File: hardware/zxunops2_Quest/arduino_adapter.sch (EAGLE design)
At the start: 8 parts

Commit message: Finalizo placa parte arduino
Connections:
- removed net D7: JP4.3
- removed net D8: JP4.2
- removed net M1+: JP4.4
- removed net M1-: JP4.5
- removed net M2+: JP5.12
- removed net M2-: JP5.11
- removed net MISO: JP5.10
- removed net N$10: JP11.5
- removed net N$6: JP11.1
- removed net N$7: JP11.2
- removed net N$8: JP11.3
- removed net N$9: JP11.4
- removed net PB1: JP4.1
- removed net SCK: JP5.9
- removed net SEN1: JP6.1
- removed net SEN10: JP6.14
- removed net SEN3: JP6.7
- removed net SEN4: JP5.8, JP6.9
- removed net SEN5: JP4.8, JP6.11
- removed net SEN6: JP6.4
- removed net SEN7: JP6.6
- removed net SEN8: JP4.6, JP6.10
- removed net SW1: JP5.7
- new net A10: JP4.7, JP6.2
- new net A11: JP4.8, JP6.1
- new net A12: JP4.5, JP6.4
- new net A13: JP4.4, JP6.5
- new net A14: JP4.2, JP6.7
- new net A15: JP4.1, JP6.8
- new net A8: JP4.3, JP6.6
- new net A9: JP4.6, JP6.3
- new net D0: JP11.1, JP5.7
- new net D1: JP11.2, JP5.8
- new net D2: JP11.3, JP5.10
- new net D4: JP11.5, JP5.12
- net 3.3V: no longer JP6.5
- net D3: now also JP11.4, JP5.11; no longer JP4.7
- net GND: now also MOUSE.3; no longer JP6.13, JP6.2, JP6.8
- net VCC: now also MOUSE.4

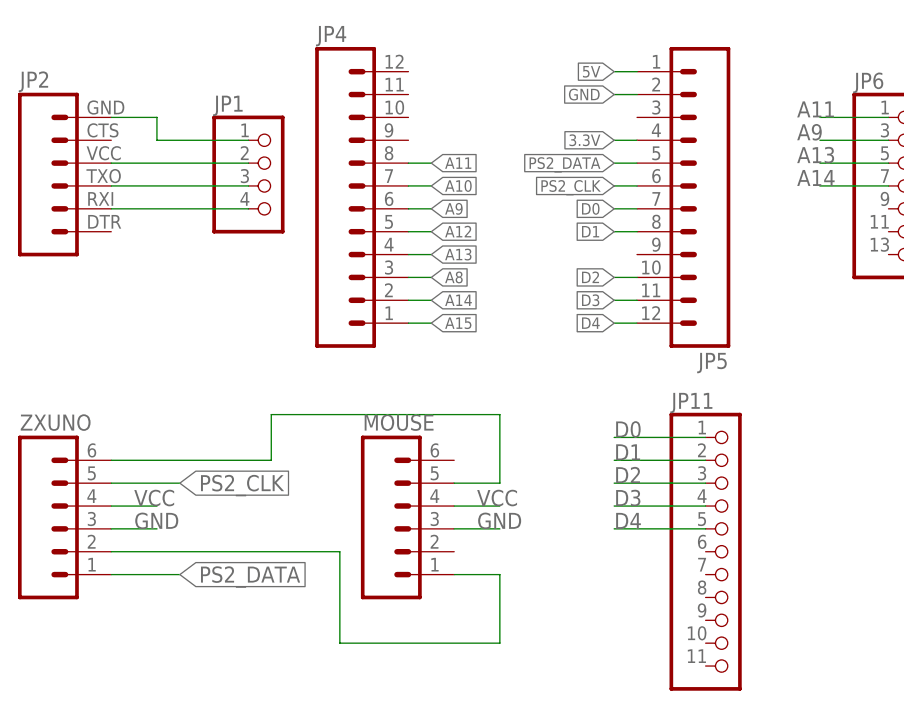
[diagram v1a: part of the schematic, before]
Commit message: 
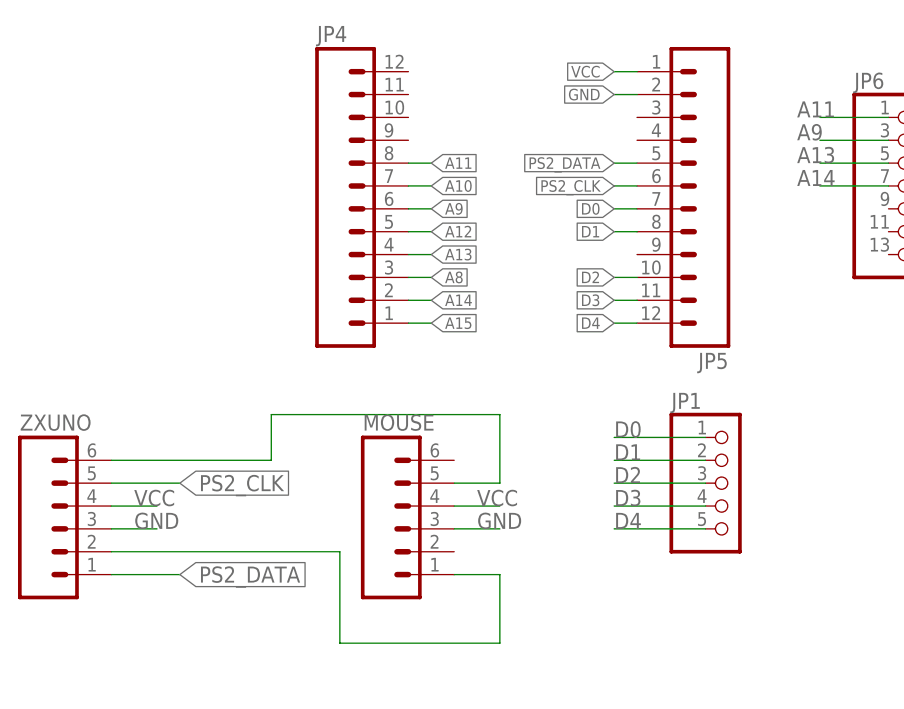
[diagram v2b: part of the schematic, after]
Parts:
- removed JP11: (no value), pinhead:PINHD-1X11
- removed JP2: (no value), SparkFun-Connectors:M06SIP
- JP1: device pinhead:PINHD-1X4 -> pinhead:PINHD-1X5
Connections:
- removed net 3.3V: JP5.4
- removed net 5V: JP5.1
- removed net N$3: JP1.1, JP2.6
- removed net N$4: JP1.2, JP2.4
- removed net N$5: JP1.3, JP2.3
- removed net TXO: JP1.4, JP2.2
- net D0: now also JP1.1; no longer JP11.1
- net D1: now also JP1.2; no longer JP11.2
- net D2: now also JP1.3; no longer JP11.3
- net D3: now also JP1.4; no longer JP11.4
- net D4: now also JP1.5; no longer JP11.5
- net VCC: now also JP5.1
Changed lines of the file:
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@@
 <part name="JP6" library="pinhead" deviceset="PINHD-2X7" device=""/>
 <part name="JP4" library="SparkFun-Connectors" deviceset="M12" device="PTH" value=""/>
-<part name="JP2" library="SparkFun-Connectors" deviceset="M06" device="SIP"/>
-<part name="JP11" library="pinhead" deviceset="PINHD-1X11" device=""/>
 <part name="ZXUNO" library="ZX_UNO_0_14" deviceset="DINC_MIN_TM_6_1" device="" value=""/>
 <part name="MOUSE" library="ZX_UNO_0_14" deviceset="DINC_MIN_TM_6_1" device="" value=""/>
-<part name="JP1" library="pinhead" deviceset="PINHD-1X4" device=""/>
+<part name="JP1" library="pinhead" deviceset="PINHD-1X5" device=""/>
 </parts>
 <sheets>
@@
 <instance part="JP6" gate="A" x="116.84" y="78.74"/>
 <instance part="JP4" gate="G$1" x="50.8" y="78.74"/>
-<instance part="JP2" gate="G$1" x="22.86" y="78.74"/>
-<instance part="JP11" gate="A" x="96.52" y="38.1"/>
 <instance part="ZXUNO" gate="G$1" x="22.86" y="40.64"/>
 <instance part="MOUSE" gate="G$1" x="60.96" y="40.64"/>
-<instance part="JP1" gate="A" x="45.72" y="78.74"/>
+<instance part="JP1" gate="A" x="96.52" y="45.72"/>
 </instances>
 <busses>
@@
 </segment>
 </net>
-<net name="5V" class="0">
-<segment>
-<wire x1="86.36" y1="91.44" x2="83.82" y2="91.44" width="0.1524" layer="91"/>
-<label x="83.82" y="91.44" size="1.27" layer="95" rot="R180" xref="yes"/>
-<pinref part="JP5" gate="G$1" pin="1"/>
-</segment>
-</net>
-<net name="TXO" class="0">
-<segment>
-<pinref part="JP2" gate="G$1" pin="2"/>
-<pinref part="JP1" gate="A" pin="4"/>
-<wire x1="27.94" y1="76.2" x2="43.18" y2="76.2" width="0.1524" layer="91"/>
-</segment>
-</net>
 <net name="A15" class="0">
 <segment>
@@
 <net name="D3" class="0">
 <segment>
-<pinref part="JP11" gate="A" pin="4"/>
 <wire x1="93.98" y1="43.18" x2="83.82" y2="43.18" width="0.1524" layer="91"/>
 <label x="83.82" y="43.18" size="1.778" layer="95"/>
+<pinref part="JP1" gate="A" pin="4"/>
 </segment>
 <segment>
@@
 <label x="83.82" y="66.04" size="1.27" layer="95" rot="R180" xref="yes"/>
 <pinref part="JP5" gate="G$1" pin="11"/>
-</segment>
-</net>
-<net name="3.3V" class="0">
-<segment>
-<wire x1="86.36" y1="83.82" x2="83.82" y2="83.82" width="0.1524" layer="91"/>
-<label x="83.82" y="83.82" size="1.27" layer="95" rot="R180" xref="yes"/>
-<pinref part="JP5" gate="G$1" pin="4"/>
 </segment>
 </net>
@@
 <pinref part="MOUSE" gate="G$1" pin="4"/>
 </segment>
-</net>
-<net name="N$3" class="0">
-<segment>
-<pinref part="JP2" gate="G$1" pin="6"/>
-<wire x1="27.94" y1="86.36" x2="33.02" y2="86.36" width="0.1524" layer="91"/>
-<wire x1="33.02" y1="86.36" x2="33.02" y2="83.82" width="0.1524" layer="91"/>
-<pinref part="JP1" gate="A" pin="1"/>
-<wire x1="33.02" y1="83.82" x2="43.18" y2="83.82" width="0.1524" layer="91"/>
-</segment>
-</net>
-<net name="N$4" class="0">
-<segment>
-<pinref part="JP2" gate="G$1" pin="4"/>
-<pinref part="JP1" gate="A" pin="2"/>
-<wire x1="27.94" y1="81.28" x2="43.18" y2="81.28" width="0.1524" layer="91"/>
-</segment>
-</net>
-<net name="N$5" class="0">
-<segment>
-<pinref part="JP2" gate="G$1" pin="3"/>
-<pinref part="JP1" gate="A" pin="3"/>
-<wire x1="27.94" y1="78.74" x2="43.18" y2="78.74" width="0.1524" layer="91"/>
+<segment>
+<wire x1="86.36" y1="91.44" x2="83.82" y2="91.44" width="0.1524" layer="91"/>
+<label x="83.82" y="91.44" size="1.27" layer="95" rot="R180" xref="yes"/>
+<pinref part="JP5" gate="G$1" pin="1"/>
 </segment>
 </net>
 <net name="D0" class="0">
 <segment>
-<pinref part="JP11" gate="A" pin="1"/>
 <wire x1="93.98" y1="50.8" x2="83.82" y2="50.8" width="0.1524" layer="91"/>
 <label x="83.82" y="50.8" size="1.778" layer="95"/>
+<pinref part="JP1" gate="A" pin="1"/>
 </segment>
 <segment>
@@
 <net name="D1" class="0">
 <segment>
-<pinref part="JP11" gate="A" pin="2"/>
 <wire x1="93.98" y1="48.26" x2="83.82" y2="48.26" width="0.1524" layer="91"/>
 <label x="83.82" y="48.26" size="1.778" layer="95"/>
+<pinref part="JP1" gate="A" pin="2"/>
 </segment>
 <segment>
@@
 <net name="D2" class="0">
 <segment>
-<pinref part="JP11" gate="A" pin="3"/>
 <wire x1="93.98" y1="45.72" x2="83.82" y2="45.72" width="0.1524" layer="91"/>
 <label x="83.82" y="45.72" size="1.778" layer="95"/>
+<pinref part="JP1" gate="A" pin="3"/>
 </segment>
 <segment>
@@
 <net name="D4" class="0">
 <segment>
-<pinref part="JP11" gate="A" pin="5"/>
 <wire x1="93.98" y1="40.64" x2="83.82" y2="40.64" width="0.1524" layer="91"/>
 <label x="83.82" y="40.64" size="1.778" layer="95"/>
-</segment>
-<segment>
+<pinref part="JP1" gate="A" pin="5"/>
+</segment>
+<segment>

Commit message: Añado proyecto buttom como referencia
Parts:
- removed JP1: (no value), pinhead:PINHD-1X5
- added JP2: (no value), pinhead:PINHD-1X11
- added U1: STM32F105RBT6, iwasz-logo:STM32F105RBT6
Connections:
- net D0: now also JP2.1; no longer JP1.1
- net D1: now also JP2.2; no longer JP1.2
- net D2: now also JP2.3; no longer JP1.3
- net D3: now also JP2.4; no longer JP1.4
- net D4: now also JP2.5; no longer JP1.5
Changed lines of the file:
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@@
 <layer number="56" name="wert" color="7" fill="1" visible="no" active="no"/>
 <layer number="57" name="tCAD" color="7" fill="1" visible="no" active="no"/>
+<layer number="58" name="bCAD" color="7" fill="1" visible="no" active="no"/>
 <layer number="90" name="Modules" color="7" fill="1" visible="yes" active="yes"/>
 <layer number="91" name="Nets" color="2" fill="1" visible="yes" active="yes"/>
@@
 <part name="ZXUNO" library="ZX_UNO_0_14" deviceset="DINC_MIN_TM_6_1" device="" value=""/>
 <part name="MOUSE" library="ZX_UNO_0_14" deviceset="DINC_MIN_TM_6_1" device="" value=""/>
-<part name="JP1" library="pinhead" deviceset="PINHD-1X5" device=""/>
+<part name="U1" library="iwasz-logo" deviceset="STM32F105RBT6" device=""/>
+<part name="JP2" library="pinhead" deviceset="PINHD-1X11" device=""/>
 </parts>
 <sheets>
@@
 <instance part="ZXUNO" gate="G$1" x="22.86" y="40.64"/>
 <instance part="MOUSE" gate="G$1" x="60.96" y="40.64"/>
-<instance part="JP1" gate="A" x="96.52" y="45.72"/>
+<instance part="U1" gate="A" x="-22.86" y="63.5"/>
+<instance part="JP2" gate="A" x="96.52" y="38.1"/>
 </instances>
 <busses>
@@
 <wire x1="93.98" y1="43.18" x2="83.82" y2="43.18" width="0.1524" layer="91"/>
 <label x="83.82" y="43.18" size="1.778" layer="95"/>
-<pinref part="JP1" gate="A" pin="4"/>
+<pinref part="JP2" gate="A" pin="4"/>
 </segment>
 <segment>
@@
 <wire x1="93.98" y1="50.8" x2="83.82" y2="50.8" width="0.1524" layer="91"/>
 <label x="83.82" y="50.8" size="1.778" layer="95"/>
-<pinref part="JP1" gate="A" pin="1"/>
+<pinref part="JP2" gate="A" pin="1"/>
 </segment>
 <segment>
@@
 <wire x1="93.98" y1="48.26" x2="83.82" y2="48.26" width="0.1524" layer="91"/>
 <label x="83.82" y="48.26" size="1.778" layer="95"/>
-<pinref part="JP1" gate="A" pin="2"/>
+<pinref part="JP2" gate="A" pin="2"/>
 </segment>
 <segment>
@@
 <wire x1="93.98" y1="45.72" x2="83.82" y2="45.72" width="0.1524" layer="91"/>
 <label x="83.82" y="45.72" size="1.778" layer="95"/>
-<pinref part="JP1" gate="A" pin="3"/>
+<pinref part="JP2" gate="A" pin="3"/>
 </segment>
 <segment>
@@
 <wire x1="93.98" y1="40.64" x2="83.82" y2="40.64" width="0.1524" layer="91"/>
 <label x="83.82" y="40.64" size="1.778" layer="95"/>
-<pinref part="JP1" gate="A" pin="5"/>
-</segment>
-<segment>
+<pinref part="JP2" gate="A" pin="5"/>
+</segment>
+<segment>
